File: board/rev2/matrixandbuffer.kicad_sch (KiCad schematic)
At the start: 4 parts, among them SW2 MS-22D28-G020, U15 74HCT245

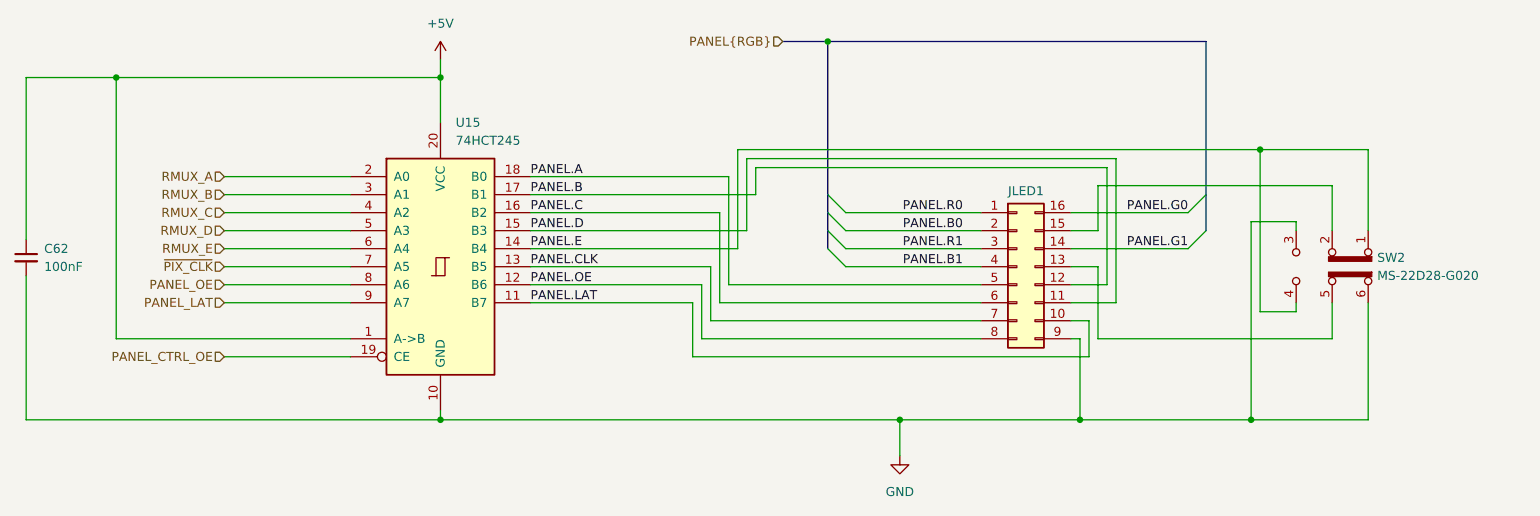
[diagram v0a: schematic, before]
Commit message: Rough full board layout
also, start re-organizing which pins of buffers/gates are used for what

still need to reorder the mem i/o lines to align better

also fix duplicate pullups and fix mem_io isolation res
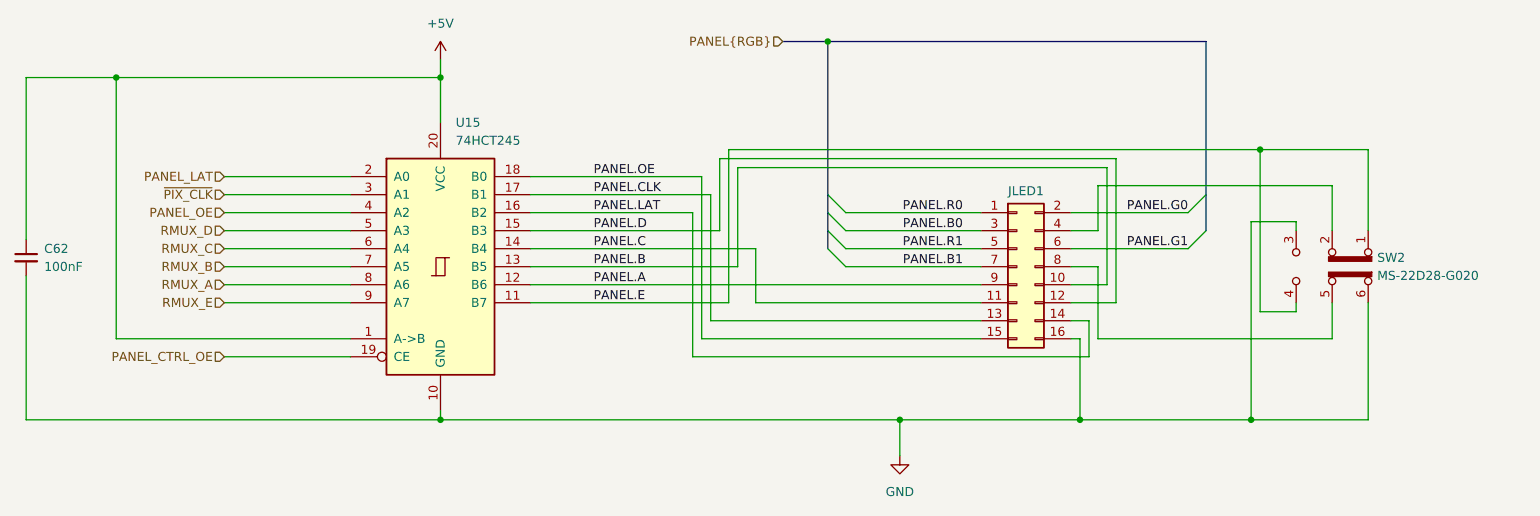
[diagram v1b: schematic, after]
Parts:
- JLED1: symbol Connector_Generic:Conn_02x08_Counter_Clockwise -> Connector_Generic:Conn_02x08_Odd_Even
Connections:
- net GND: now also JLED1.16 (Pin_16); no longer JLED1.9 (Pin_9)
- net PANEL.A: now also JLED1.9 (Pin_9), U15.12 (B6); no longer JLED1.5 (Pin_5), U15.18 (B0)
- net PANEL.B: now also JLED1.10 (Pin_10), U15.13 (B5); no longer JLED1.12 (Pin_12), U15.17 (B1)
- net PANEL.B0: now also JLED1.3 (Pin_3); no longer JLED1.2 (Pin_2)
- net PANEL.B1: now also JLED1.7 (Pin_7); no longer JLED1.4 (Pin_4)
- net PANEL.C: now also JLED1.11 (Pin_11), U15.14 (B4); no longer JLED1.6 (Pin_6), U15.16 (B2)
- net PANEL.CLK: now also JLED1.13 (Pin_13), U15.17 (B1); no longer JLED1.7 (Pin_7), U15.13 (B5)
- net PANEL.D: now also JLED1.12 (Pin_12); no longer JLED1.11 (Pin_11)
- net PANEL.E: now also U15.11 (B7); no longer U15.14 (B4)
- net PANEL.G0: now also JLED1.2 (Pin_2); no longer JLED1.16 (Pin_16)
- net PANEL.G1: now also JLED1.6 (Pin_6); no longer JLED1.14 (Pin_14)
- net PANEL.LAT: now also JLED1.14 (Pin_14), U15.16 (B2); no longer JLED1.10 (Pin_10), U15.11 (B7)
- net PANEL.OE: now also JLED1.15 (Pin_15), U15.18 (B0); no longer JLED1.8 (Pin_8), U15.12 (B6)
- net PANEL.R1: now also JLED1.5 (Pin_5); no longer JLED1.3 (Pin_3)
- net PANEL_LAT: now also U15.2 (A0); no longer U15.9 (A7)
- net PANEL_OE: now also U15.4 (A2); no longer U15.8 (A6)
- net RMUX_A: now also U15.8 (A6); no longer U15.2 (A0)
- net RMUX_B: now also U15.7 (A5); no longer U15.3 (A1)
- net RMUX_C: now also U15.6 (A4); no longer U15.4 (A2)
- net RMUX_E: now also U15.9 (A7); no longer U15.6 (A4)
- net ~{PIX_CLK}: now also U15.3 (A1); no longer U15.7 (A5)
- net at SW2.2 (B): now also JLED1.4 (Pin_4); no longer JLED1.15 (Pin_15)
- net at SW2.5 (B): now also JLED1.8 (Pin_8); no longer JLED1.13 (Pin_13)

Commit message: Finish board rev2
woo another pcb
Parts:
- SW2: value MS-22D28-G020 -> MS-22D17AG2.5-B; footprint Switch_Slide_SMD:SW-SMD_MS-22D28-G020 -> Switch_Slide_SMD:SW-SMD_MS-22D17AG2.5; LCSC C963205 -> C20611671; Part MS-22D28-G020 -> MS-22D17AG2.5-B
